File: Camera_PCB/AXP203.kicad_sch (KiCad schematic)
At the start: 39 parts, among them J3 USB_C_Receptacle_PowerOnly_6P, SW1 PWR, SW2 RST, U1 AXP203

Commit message: cleaned up Camera_PCB \repository
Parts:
- added C80: 1u, Capacitor_SMD:C_0603_1608Metric_Pad1.08x0.95mm_HandSolder, symbol Device:C_Small
- added D1: LED_RGB, BackupCamCustomParts:RGB_LED IN-S66TFT5R5G5B, symbol Device:LED_RGB
- added R18: 47k, Resistor_SMD:R_0603_1608Metric_Pad0.98x0.95mm_HandSolder, symbol Device:R_Small_US
- added R19, R28, R29: 470, Resistor_SMD:R_0603_1608Metric_Pad0.98x0.95mm_HandSolder, symbol Device:R_Small_US
- C35, C42, C43, C50, C54, C56, C58, C6, C62, C63: footprint (none) -> Capacitor_SMD:C_0805_2012Metric_Pad1.18x1.45mm_HandSolder; DPN (none) -> GRM21BZ71E106KE15L; Distributor (none) -> DigiKey
- C36: value 4.7u -> 10u; footprint (none) -> Capacitor_SMD:C_0805_2012Metric_Pad1.18x1.45mm_HandSolder; DPN (none) -> GRM21BZ71E106KE15L; Distributor (none) -> DigiKey
- C44, C61, C73, C74: footprint (none) -> Capacitor_SMD:C_0805_2012Metric_Pad1.18x1.45mm_HandSolder; DPN (none) -> GRM21BZ71H475ME15K; Distributor (none) -> DigiKey
- C45, C59, C60: footprint (none) -> Capacitor_SMD:C_0603_1608Metric_Pad1.08x0.95mm_HandSolder; DPN (none) -> GRM188R72A104KA35D; Distributor (none) -> DigiKey
- C48, C49, C5: footprint (none) -> Capacitor_SMD:C_0603_1608Metric_Pad1.08x0.95mm_HandSolder; DPN (none) -> GCM188R71E105KA64D; Distributor (none) -> DigiKey
- C55, C57: value 0.1u -> 1n; footprint (none) -> Capacitor_SMD:C_0603_1608Metric_Pad1.08x0.95mm_HandSolder; DPN (none) -> GRM1885C1H102JA01D; Distributor (none) -> DigiKey
- L5, L8, L9: footprint (none) -> Inductor_SMD:L_TDK_SLF6045; DPN (none) -> SLF6045T-4R7N2R4-3PF; Distributor (none) -> DigiKey
- R14: footprint (none) -> Resistor_SMD:R_1206_3216Metric; DPN (none) -> PE1206DRM070R03L; Distributor (none) -> DigiKey
- R15: footprint (none) -> Resistor_SMD:R_0603_1608Metric_Pad0.98x0.95mm_HandSolder; DPN (none) -> RC0603FR-07200KL; Distributor (none) -> DigiKey
- R16, R17: footprint (none) -> Resistor_SMD:R_0603_1608Metric_Pad0.98x0.95mm_HandSolder; DPN (none) -> RC0603FR-075K1L; Distributor (none) -> DigiKey
- R20, R21: footprint (none) -> Resistor_SMD:R_0603_1608Metric_Pad0.98x0.95mm_HandSolder; DPN (none) -> RC0603FR-101KL; Distributor (none) -> DigiKey
- R22, R23: footprint (none) -> Resistor_SMD:R_0603_1608Metric_Pad0.98x0.95mm_HandSolder; DPN (none) -> RC0603JR-070RL; Distributor (none) -> DigiKey
- SW1, SW2: footprint (none) -> Button_Switch_SMD:SW_SPST_PTS647_Sx38; DPN (none) -> Y97KT23B5NAFP; Distributor (none) -> DigiKey
- U1: Distributor (none) -> AliExpress
- renumbered J3 to J6
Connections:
- net CHGLED: now also D1.2 (GK)
- net GND: now also C59.2, C60.2, R23.1, SW1.2, SW2.2, C80.2, D1.1 (RK), D1.3 (BK)
- net GNDA: no longer C59.2, C60.2, R23.1, SW1.2, SW2.2
- net PGOOD: now also C80.1, R18.2, R19.1
- net VCC-RTC: now also R18.1
- net VIPS: now also R28.1
- new net: D1.4 (BA), R19.2
- new net: D1.5 (GA), R28.2
- new net: D1.6 (RA), R29.2
- new net STATUS_LED: R29.1
- no-connect marks 7 -> 12
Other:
- note added: "1.2V rail is 1.25V Supplies VDD-CPU, VDD-SYS max 900mA"
- note added: "1.8V Supplies VDD-DRAM max 600mA"
- note added: "3.0V"
- note added: "Always on 3.3v"
- note added: "Status LED Green = booted Blue = power on Red = charging"
- note added: "USB Power Header"
- note added: "use 1nF caps as filter caps for feedback pins place close to IC"
- note removed: "VCC-RTC is 3.3V"
- moved on the sheet: BT1, C35, C36, C42, C43, C44, C45, C48, C49, C5, C50, C54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

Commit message: Thorough Camera PCB Review by Jack
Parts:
- removed SW1: PWR, Button_Switch_SMD:SW_SPST_PTS647_Sx38, symbol Switch:SW_MEC_5E
- removed SW2: RST, Button_Switch_SMD:SW_SPST_PTS647_Sx38, symbol Switch:SW_MEC_5E
- added NT1: NetTie_2, NetTie:NetTie-2_SMD_Pad2.0mm, symbol Device:NetTie_2
- added NT2: NetTie_2, NetTie:NetTie-2_SMD_Pad0.5mm, symbol Device:NetTie_2
- added SW1: PWR, Button_Switch_SMD:SW_SPST_PTS647_Sx38, symbol Switch:SW_Push
- added SW2: RST, Button_Switch_SMD:SW_SPST_PTS647_Sx38, symbol Switch:SW_Push
- added TP1: VBAT, TestPoint:TestPoint_Pad_D1.5mm, symbol Connector:TestPoint
- added TP10: RST, TestPoint:TestPoint_Pad_D1.5mm, symbol Connector:TestPoint
- added TP11: STAT, TestPoint:TestPoint_Pad_D1.5mm, symbol Connector:TestPoint
- added TP12: PON, TestPoint:TestPoint_Pad_D1.5mm, symbol Connector:TestPoint
- added TP13: NOE, TestPoint:TestPoint_Pad_D1.5mm, symbol Connector:TestPoint
- added TP16, TP7: 3.0V, TestPoint:TestPoint_Pad_D1.5mm, symbol Connector:TestPoint
- added TP17: SCK0, TestPoint:TestPoint_Pad_D1.5mm, symbol Connector:TestPoint
- added TP18: SDA0, TestPoint:TestPoint_Pad_D1.5mm, symbol Connector:TestPoint
- added TP19: PEN, TestPoint:TestPoint_Pad_D1.5mm, symbol Connector:TestPoint
- added TP2: VIPS, TestPoint:TestPoint_Pad_D1.5mm, symbol Connector:TestPoint
- added TP20: CHS, TestPoint:TestPoint_Pad_D1.5mm, symbol Connector:TestPoint
- added TP3: 1V2, TestPoint:TestPoint_Pad_D1.5mm, symbol Connector:TestPoint
- added TP4: 1V8, TestPoint:TestPoint_Pad_D1.5mm, symbol Connector:TestPoint
- added TP5: VBUS, TestPoint:TestPoint_Pad_D1.5mm, symbol Connector:TestPoint
- added TP6: VINT, TestPoint:TestPoint_Pad_D1.5mm, symbol Connector:TestPoint
- added TP8: VRTC, TestPoint:TestPoint_Pad_D1.5mm, symbol Connector:TestPoint
- added TP9: PGOOD, TestPoint:TestPoint_Pad_D1.5mm, symbol Connector:TestPoint
- BT1: value Battery_Cell -> B2B-PH-SM4-TB; footprint (none) -> Connector_JST:JST_PH_B2B-PH-SM4-TB_1x02-1MP_P2.00mm_Vertical; DPN (none) -> B2B-PH-SM4-TB; Distributor (none) -> DigiKey
- J6: footprint Connector_USB:USB_C_Receptacle_GCT_USB4085 -> Connector_USB:USB_C_Receptacle_GCT_USB4125-xx-x_6P_TopMnt_Horizontal; DPN USB4085-GF-A -> USB4125-GF-A
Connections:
- net +1V2: now also TP3.1
- net +1V8: now also TP4.1
- net +3V0: now also TP7.1
- net GND: now also NT1.2, SW1.1, SW2.1
- net GNDA: now also NT1.1
- net PGOOD: now also NT2.1, TP9.1; no longer C80.1, R18.2
- net PWREN: now also TP19.1
- net STATUS_LED: now also TP11.1
- net TWI0_SCK: now also TP17.1
- net TWI0_SDA: now also TP18.1
- net VBAT: now also TP1.1
- net VBUS: now also TP5.1
- net VCC-RTC: now also TP8.1
- net VINT: now also TP6.1
- net VIPS: now also TP2.1
- net at C5.2, C6.1, L5.2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: now also TP20.1
- net at R21.1: now also SW2.2
- net at C60.1, R21.2, U1.4 (N_OE): now also TP13.1
- net at C59.1, R20.2, U1.47 (PWRON): now also TP12.1
- net at R22.2, R23.2, U1.6 (N_VBUSEN): now also TP16.1
- net at R20.1: now also SW1.2
- new net RESET: C80.1, NT2.2, R18.2, TP10.1
- no-connect marks 12 -> 8
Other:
- note added: "3.7V Lithium Ion Battery W/ built in UV/OC protection Target 8Ah. Board PN is standard 2.0mm RC Battery Connector, PH series from JST"
- note removed: "3.0V"
- note removed: "3.7V Lithium Ion Battery W/ built in UV/OC protection Target 8Ah"
- moved on the sheet: L5

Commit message: more schematic changes, added solder bridges, etc
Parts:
- added JP1, JP2, JP3, JP4: ~, Jumper:SolderJumper-2_P1.3mm_Open_Pad1.0x1.5mm, symbol Jumper:Jumper_2_Small_Bridged
- NT1: footprint NetTie:NetTie-2_SMD_Pad2.0mm -> NetTie:NetTie-2_SMD_Pad0.5mm
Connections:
- net +1V2: now also JP3.2 (B); no longer C54.2, C55.2, L8.2, TP3.1, U1.10 (DCDC2)
- net +1V8: now also JP4.2 (B); no longer C56.2, C57.2, L9.2, TP4.1, U1.17 (DCDC3)
- net +3V0: now also JP2.2 (B); no longer C63.2, U1.12 (LD02)
- net VCC-RTC: now also JP1.2 (B); no longer C61.2, TP8.1, U1.28 (LDO1)
- new net: C56.2, C57.2, JP4.1 (A), L9.2, TP4.1, U1.17 (DCDC3)
- new net: C63.2, JP2.1 (A), U1.12 (LD02)
- new net: C54.2, C55.2, JP3.1 (A), L8.2, TP3.1, U1.10 (DCDC2)
- new net: C61.2, JP1.1 (A), TP8.1, U1.28 (LDO1)
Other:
- moved on the sheet: C56, C57, TP7

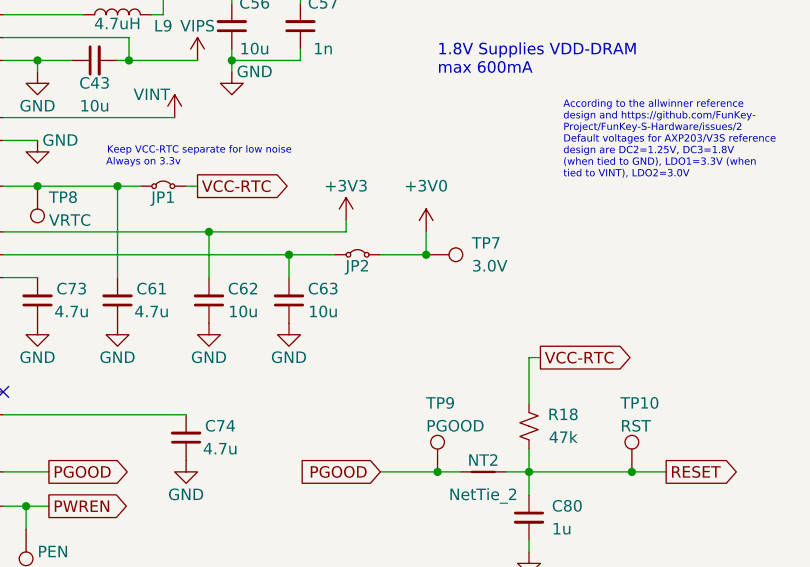
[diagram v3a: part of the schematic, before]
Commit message: PCB commit before reorganizing
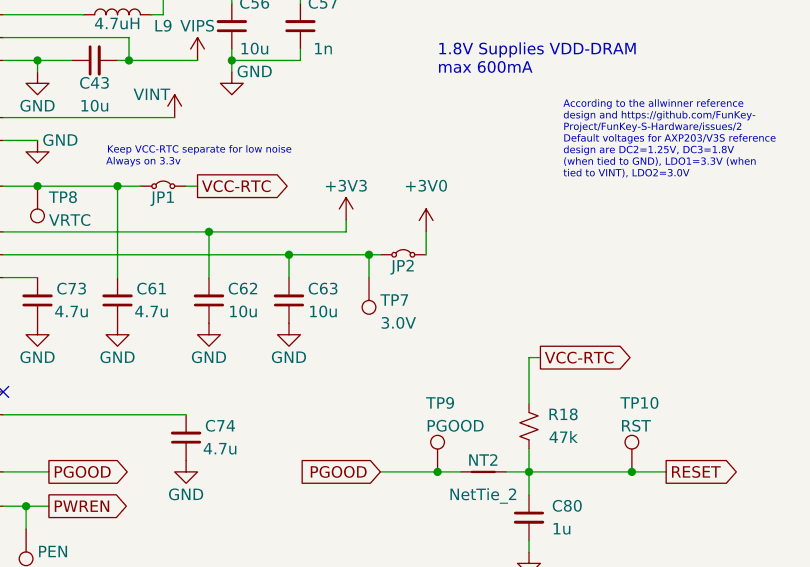
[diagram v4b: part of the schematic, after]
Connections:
- net +3V0: no longer TP7.1
- net at C63.2, JP2.1 (A), U1.12 (LD02): now also TP7.1
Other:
- moved on the sheet: JP2, TP7
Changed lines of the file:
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@@
 	)
 	(junction
-		(at 241.3 118.11)
-		(diameter 0)
-		(color 0 0 0 0)
-	)
-	(junction
 		(at 156.21 144.78)
 		(diameter 0)
@@
 	)
 	(junction
+		(at 234.95 118.11)
+		(diameter 0)
+		(color 0 0 0 0)
+	)
+	(junction
 		(at 153.67 97.79)
 		(diameter 0)
@@
 	(wire
 		(pts
+			(xy 234.95 118.11) (xy 236.22 118.11)
+		)
+		(stroke
+			(width 0)
+			(type default)
+		)
+	)
+	(wire
+		(pts
 			(xy 54.61 111.76) (xy 54.61 114.3)
 		)
@@
 	(wire
 		(pts
+			(xy 234.95 120.65) (xy 234.95 118.11)
+		)
+		(stroke
+			(width 0)
+			(type default)
+		)
+	)
+	(wire
+		(pts
 			(xy 156.21 60.96) (xy 156.21 63.5)
 		)
@@
 	(wire
 		(pts
-			(xy 236.22 118.11) (xy 241.3 118.11)
-		)
-		(stroke
-			(width 0)
-			(type default)
-		)
-	)
-	(wire
-		(pts
 			(xy 124.46 167.64) (xy 118.11 167.64)
 		)
@@
 	(wire
 		(pts
-			(xy 226.06 118.11) (xy 231.14 118.11)
+			(xy 226.06 118.11) (xy 234.95 118.11)
 		)
 		(stroke
@@
 	(symbol
 		(lib_id "Jumper:Jumper_2_Small_Bridged")
-		(at 233.68 118.11 0)
+		(at 238.76 118.11 0)
 		(unit 1)
 		(exclude_from_sim no)
@@
 		(dnp no)
 		(property "Reference" "JP2"
-			(at 233.68 119.38 0)
+			(at 238.76 119.38 0)
 			(effects
 				(font
@@
 		)
 		(property "Value" "~"
-			(at 233.68 115.57 0)
+			(at 238.76 115.57 0)
 			(effects
 				(font
@@
 		)
 		(property "Footprint" "Jumper:SolderJumper-2_P1.3mm_Open_Pad1.0x1.5mm"
-			(at 233.68 118.11 0)
+			(at 238.76 118.11 0)
 			(effects
 				(font
@@
 		)
 		(property "Datasheet" "~"
-			(at 233.68 118.11 0)
+			(at 238.76 118.11 0)
 			(effects
 				(font
@@
 		)
 		(property "Description" "Jumper, 2-pole, small symbol, bridged"
-			(at 233.68 118.11 0)
+			(at 238.76 118.11 0)
 			(effects
 				(font
@@
 	(symbol
 		(lib_id "Connector:TestPoint")
-		(at 241.3 118.11 270)
+		(at 234.95 120.65 180)
 		(unit 1)
 		(exclude_from_sim no)
@@
 		(dnp no)
 		(property "Reference" "TP7"
-			(at 246.38 116.84 90)
+			(at 236.22 123.19 0)
 			(effects
 				(font
 					(size 1.27 1.27)
 				)
-				(justify left)
+				(justify right)
 			)
 		)
 		(property "Value" "3.0V"
-			(at 246.38 119.38 90)
+			(at 236.22 125.73 0)
 			(effects
 				(font
 					(size 1.27 1.27)
 				)
-				(justify left)
+				(justify right)
 			)
 		)
 		(property "Footprint" "TestPoint:TestPoint_Pad_D1.5mm"
-			(at 241.3 123.19 0)
+			(at 229.87 120.65 0)
 			(effects
 				(font
@@
 		)
 		(property "Datasheet" "~"
-			(at 241.3 123.19 0)
+			(at 229.87 120.65 0)
 			(effects
 				(font
@@
 		)
 		(property "Description" "test point"
-			(at 241.3 118.11 0)
+			(at 234.95 120.65 0)
 			(effects
 				(font

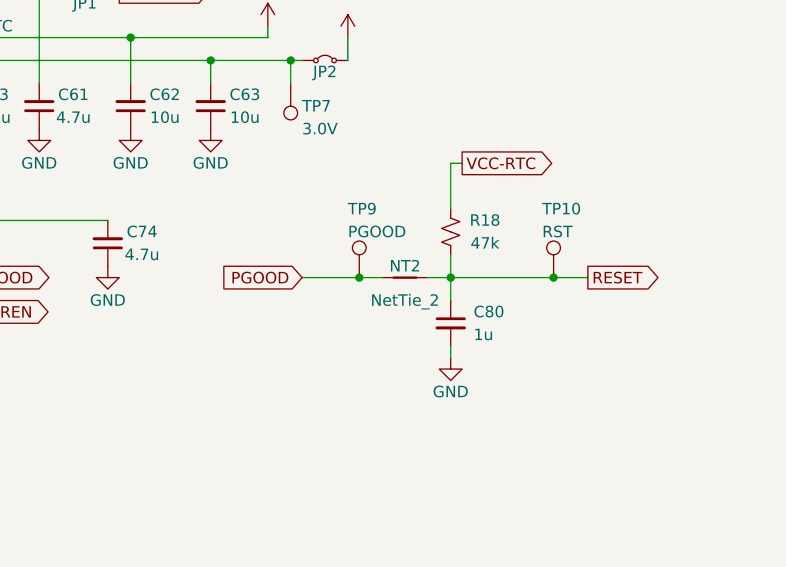
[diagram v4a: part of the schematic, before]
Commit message: Shrunk camera PCB and rearranged connectors. Everything on board. Not everything connected.
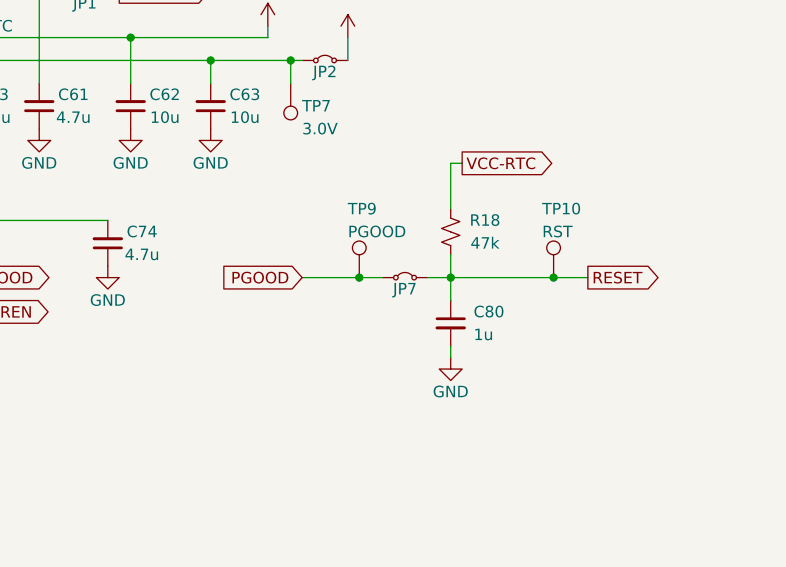
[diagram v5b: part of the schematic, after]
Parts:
- removed NT2: NetTie_2, NetTie:NetTie-2_SMD_Pad0.5mm, symbol Device:NetTie_2
- added JP7: ~, Jumper:SolderJumper-2_P1.3mm_Open_Pad1.0x1.5mm, symbol Jumper:Jumper_2_Small_Bridged
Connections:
- net PGOOD: now also JP7.1 (A)
- net RESET: now also JP7.2 (B)
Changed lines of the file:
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@@
+	)
+	(symbol
+		(lib_id "Jumper:Jumper_2_Small_Bridged")
+		(at 247.65 142.24 0)
+		(unit 1)
+		(exclude_from_sim no)
+		(in_bom yes)
+		(on_board yes)
+		(dnp no)
+		(property "Reference" "JP7"
+			(at 247.65 143.51 0)
+			(effects
+				(font
+					(size 1.27 1.27)
+				)
+			)
+		)
+		(property "Value" "~"
+			(at 247.65 139.7 0)
+			(effects
+				(font
+					(size 1.27 1.27)
+				)
+			)
+		)
+		(property "Footprint" "Jumper:SolderJumper-2_P1.3mm_Open_Pad1.0x1.5mm"
+			(at 247.65 142.24 0)
+			(effects
+				(font
+					(size 1.27 1.27)
+				)
+				(hide yes)
+			)
+		)
+		(property "Datasheet" "~"
+			(at 247.65 142.24 0)
+			(effects
+				(font
+					(size 1.27 1.27)
+				)
+				(hide yes)
+			)
+		)
+		(property "Description" "Jumper, 2-pole, small symbol, bridged"
+			(at 247.65 142.24 0)
+			(effects
+				(font
+					(size 1.27 1.27)
+				)
+				(hide yes)
+			)
+		)
+		(pin "2"
+		)
+		(pin "1"
+		)
+		(instances
+			(project "CameraPCB"
+				(path "/400c1603-202c-4359-a830-d2f0d06dd3ce/63007821-20b4-4692-9a5a-85c4738356da"
+					(reference "JP7")
+					(unit 1)
+				)
+			)
+		)
 	)
 	(symbol
@@
 					(unit 1)
 				)
-			)
-		)
-	)
-	(symbol
-		(lib_id "Device:NetTie_2")
-		(at 247.65 142.24 0)
-		(unit 1)
-		(exclude_from_sim no)
-		(in_bom no)
-		(on_board yes)
-		(dnp no)
-		(property "Reference" "NT2"
-			(at 247.65 140.97 0)
-			(effects
-				(font
-					(size 1.27 1.27)
-				)
-			)
-		)
-		(property "Value" "NetTie_2"
-			(at 247.65 144.78 0)
-			(effects
-				(font
-					(size 1.27 1.27)
-				)
-			)
-		)
-		(property "Footprint" "NetTie:NetTie-2_SMD_Pad0.5mm"
-			(at 247.65 142.24 0)
-			(effects
-				(font
-					(size 1.27 1.27)
-				)
-				(hide yes)
-			)
-		)
-		(property "Datasheet" "~"
-			(at 247.65 142.24 0)
-			(effects
-				(font
-					(size 1.27 1.27)
-				)
-				(hide yes)
-			)
-		)
-		(property "Description" "Net tie, 2 pins"
-			(at 247.65 142.24 0)
-			(effects
-				(font
-					(size 1.27 1.27)
-				)
-				(hide yes)
-			)
-		)
-		(pin "1"
-		)
-		(pin "2"
-		)
-		(instances
-			(project "CameraPCB"
-				(path "/400c1603-202c-4359-a830-d2f0d06dd3ce/63007821-20b4-4692-9a5a-85c4738356da"
-					(reference "NT2")
-					(unit 1)
-				)
